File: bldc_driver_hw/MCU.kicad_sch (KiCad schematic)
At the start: 34 parts, among them SW1 SW_Push, U5 MCP1501-33xSN, U6 STM32G474RETx, Y1 24MHz

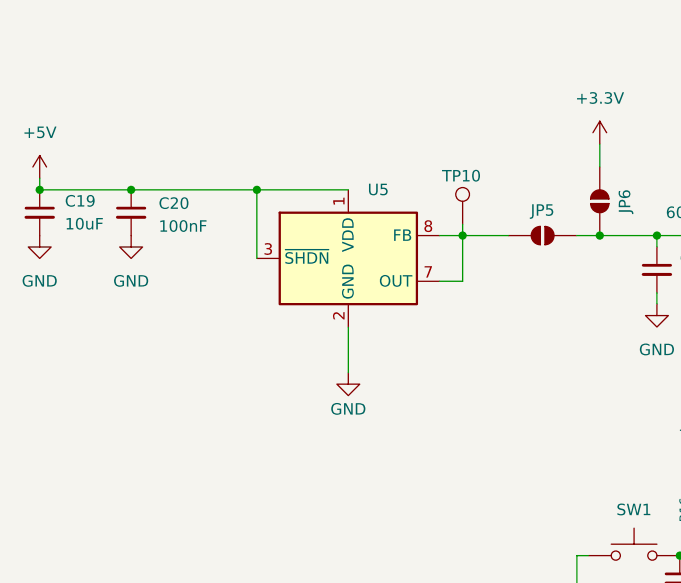
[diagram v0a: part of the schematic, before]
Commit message: changed vref
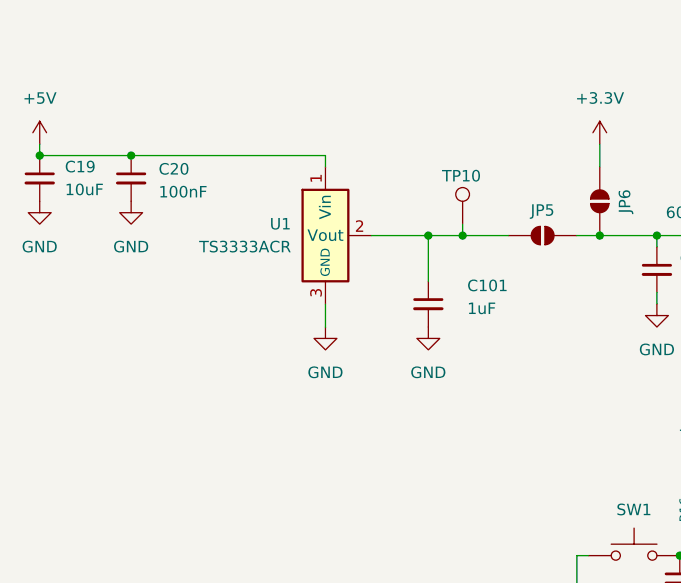
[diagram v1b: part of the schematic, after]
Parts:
- removed U5: MCP1501-33xSN, Package_SO:SOIC-8_3.9x4.9mm_P1.27mm, symbol Reference_Voltage:MCP1501-33xSN
- added C101: 1uF, Capacitor_SMD:C_0603_1608Metric, symbol Device:C_Small
- added U1: TS3333ACR, Package_TO_SOT_SMD:SOT-23-3, symbol Reference_Voltage:LT1790-5
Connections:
- net +5V: now also U1.1 (Vin)
- net GND: now also C101.2, U1.3 (GND)
- net at JP5.1 (A), TP10.1: now also C101.1, U1.2 (Vout)
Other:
- moved on the sheet: C19, C20

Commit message: changed hrtim to tim1
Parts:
- removed JP7, JP8: SolderJumper_2_Open, Jumper:SolderJumper-2_P1.3mm_Open_RoundedPad1.0x1.5mm, symbol Jumper:SolderJumper_2_Open
- U1: now left out of the parts list
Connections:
- net H_BRIDGE_IRQ is gone; now on net IN_L_U: U6.37 (PB15)
- net B_H_SENS_U: now also U6.23 (PC5); no longer U6.36 (PB14)
- net B_H_SENS_V: now also U6.19 (PA5); no longer U6.35 (PB13)
- net B_H_SENS_W: now also U6.18 (PA4); no longer U6.34 (PB12)
- net IN_H_U: now also U6.44 (PA10); no longer U6.43 (PA9)
- net IN_H_V: now also U6.43 (PA9); no longer U6.41 (PC9)
- net IN_H_W: now also U6.42 (PA8); no longer U6.39 (PC7)
- net IN_L_U: no longer U6.42 (PA8)
- net IN_L_V: now also U6.36 (PB14); no longer U6.40 (PC8)
- net IN_L_W: now also U6.35 (PB13); no longer U6.38 (PC6)
- net UART_MOTOR_RX: now also U6.60 (PB7)
- net UART_MOTOR_TX: now also U6.59 (PB6)
- no-connect marks 16 -> 17
